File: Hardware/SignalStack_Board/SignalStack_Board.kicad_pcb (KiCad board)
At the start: 2 copper layers, 92.6 x 80.4 mm, 76 parts, among them J2 RJ45_LED_Shielded, J3 Molex_uF_SV_06, Q1 SI4156DY, Q2 SI4156DY, Q3 SI4156DY, Q4 SI4156DY, Q5 SI4156DY, Q6 SI4156DY, Q7 SI4156DY, Q8 SI4156DY, Q9 Q_PMOS_DGS, SW1 SW_Push, SW2 SW_Push, U1 OKI, U10 74LVC2G04, U2 SMAJ12CA, U3 Teensy4.1_DEV-16771, U4 TSR_1-2450, U5 IRS2005S, U6 IRS2005S, U7 74LVC2G04, U8 IRS2005S, U9 IRS2005S

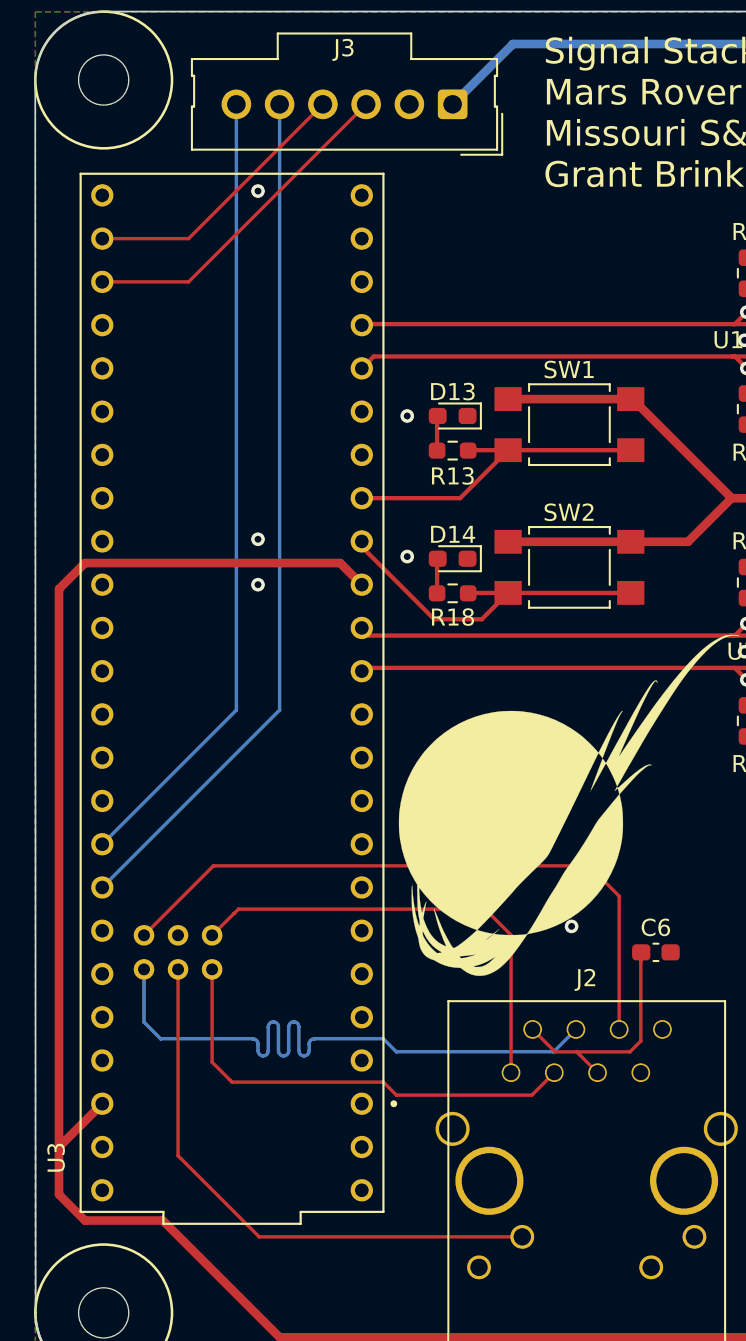
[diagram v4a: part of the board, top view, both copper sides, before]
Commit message: Added pull up resistors
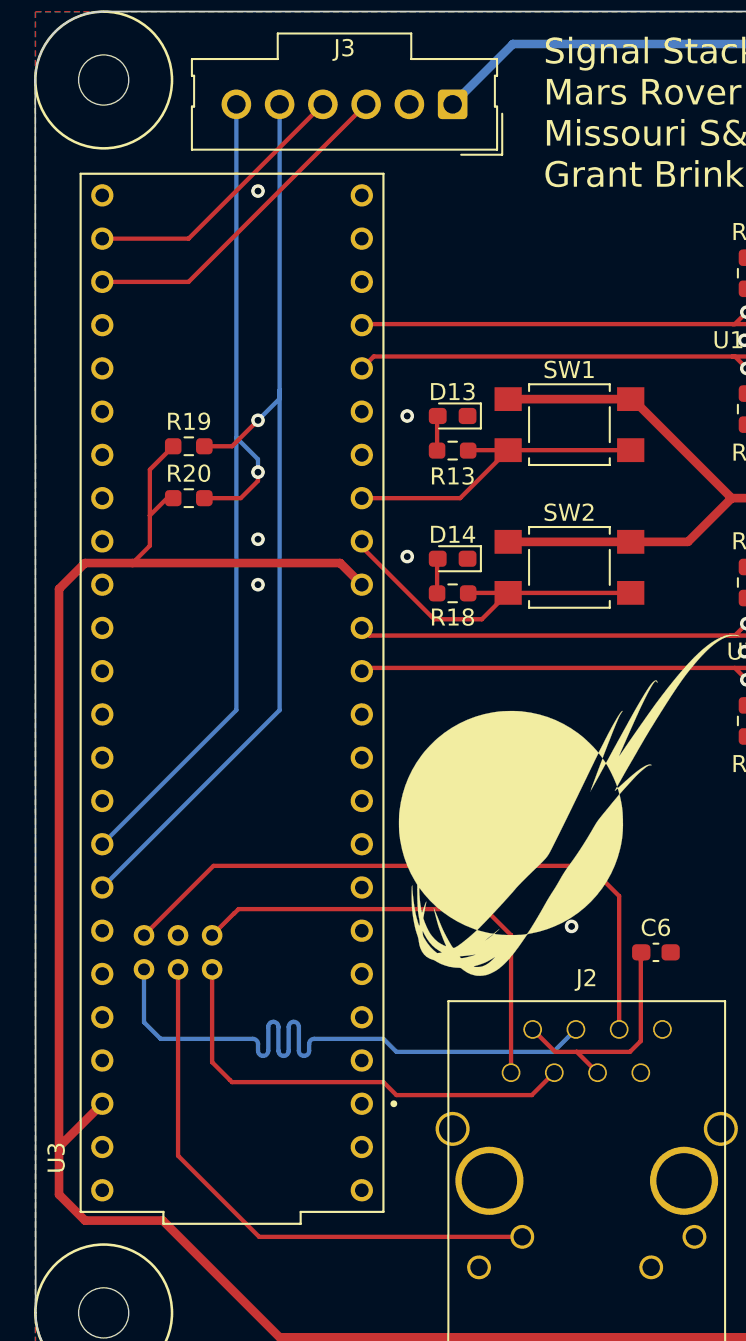
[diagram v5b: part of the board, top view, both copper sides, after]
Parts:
- added R19: 4.7k, Resistor_SMD:R_0603_1608Metric_Pad0.98x0.95mm_HandSolder, F.Cu at (121.4, 83.6)
- added R20: 4.7k, Resistor_SMD:R_0603_1608Metric_Pad0.98x0.95mm_HandSolder, F.Cu at (121.4, 86.6)
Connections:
- U3 pad R-: /RX- -> (no net)
- U3 pad T-: /TX- -> (no net)
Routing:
- net +3V3: track 261.2 -> 270.9 mm
- net I2C SDA: track 46.7 -> 53.3 mm, vias 0 -> 1
- net I2C SCL: track 50.3 -> 56.4 mm, vias 0 -> 1

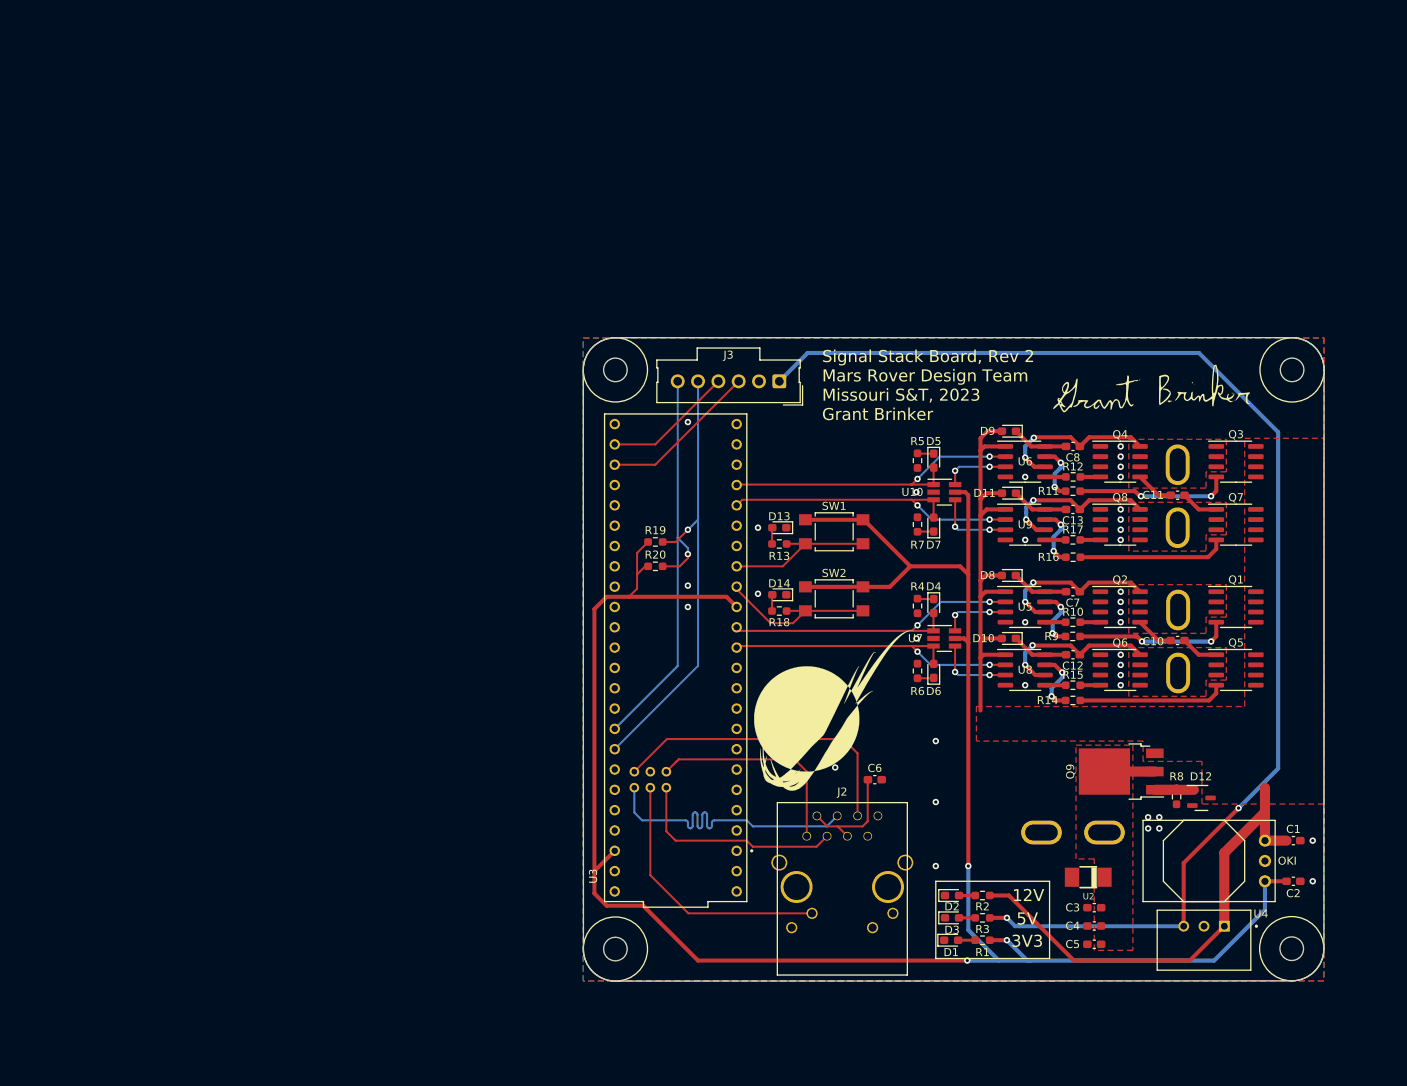
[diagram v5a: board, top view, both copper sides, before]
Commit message: Edited Signal Stack Board to be smaller
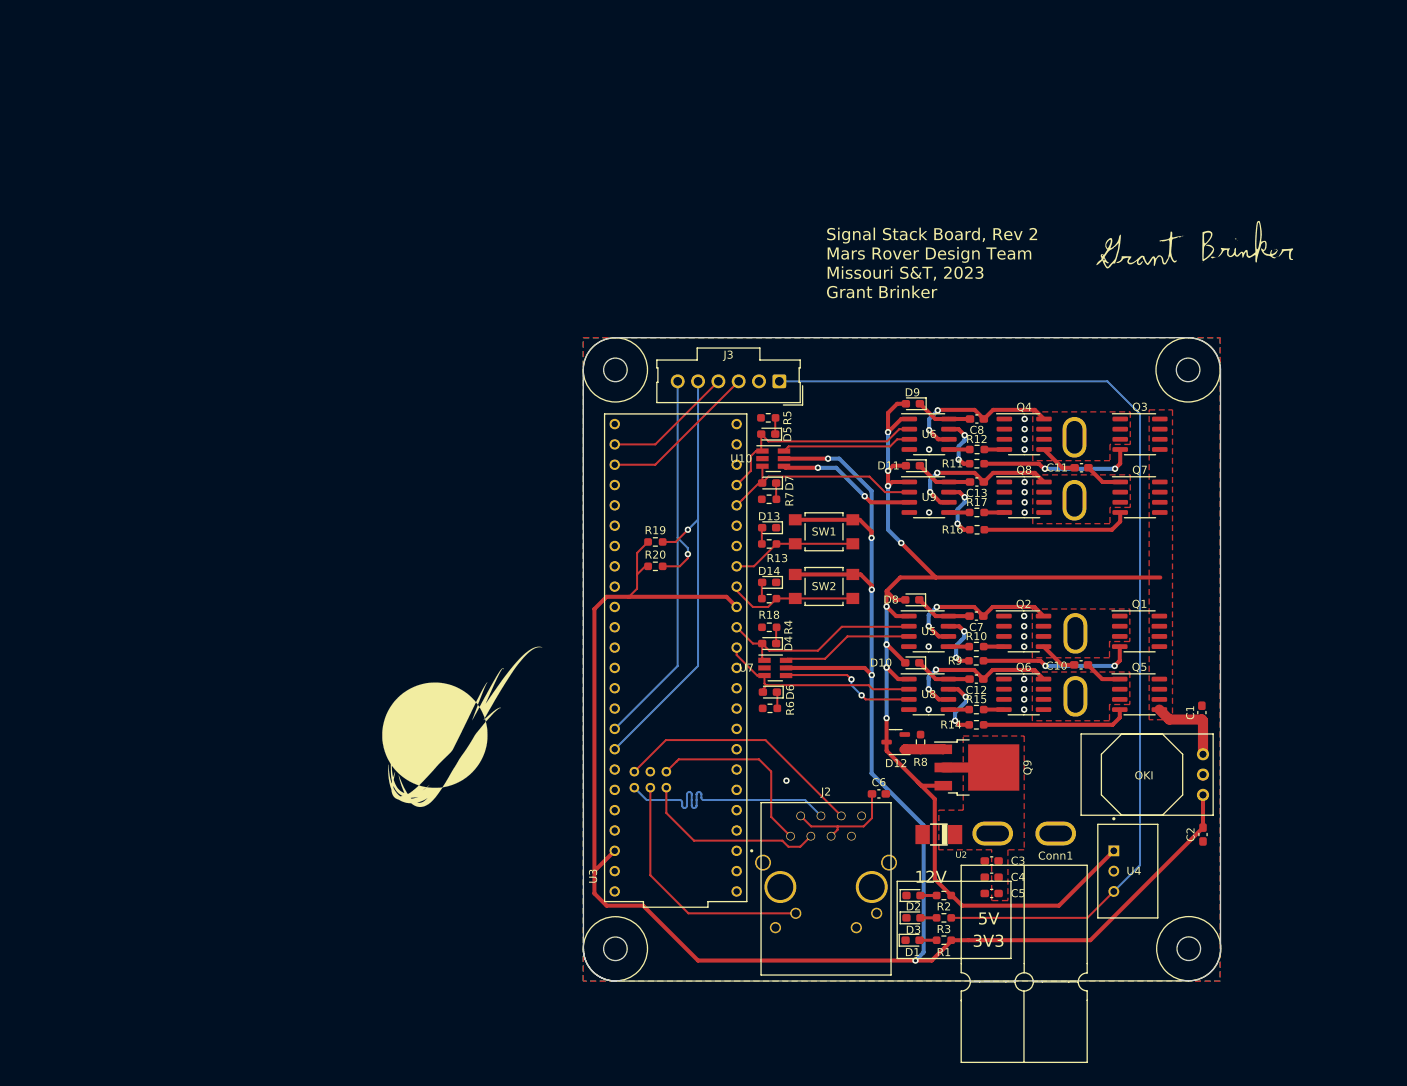
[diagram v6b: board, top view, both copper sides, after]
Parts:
- Conn1: moved to B.Cu
- moved G*** 46.5 mm to (97.3, 106.7)
- moved D12 38.9 mm to (151.4, 108.6), turned to 180 degrees
- moved R8 32.7 mm to (154.6, 108.6), turned to -90 degrees
- moved U10 21.8 mm to (136.1, 73.2)
- moved U7 21.4 mm to (136.4, 99.3)
- moved D7 21.2 mm to (135.6, 76.2), turned to 180 degrees
- moved D4 21.1 mm to (135.6, 96.3), turned to 180 degrees
- moved D5 21.0 mm to (135.5, 70.1), turned to 180 degrees
- moved D6 20.7 mm to (135.7, 102.3), turned to 180 degrees
- moved C1 19.7 mm to (189.7, 104.9), turned to 90 degrees
- moved U2 19.4 mm to (156.8, 120.1)
- moved R5 19.4 mm to (135.5, 68.1), turned to 0 degrees
- moved R6 19.0 mm to (135.7, 104.4), turned to 0 degrees
- moved R7 18.8 mm to (135.6, 78.2), turned to 0 degrees
- moved G*** 18.8 mm to (189.0, 46.5)
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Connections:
- U3 pad R-: (no net) -> /RX-
- U3 pad T-: (no net) -> /TX-
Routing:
- net +12V: track 119.3 -> 160.8 mm, vias 0 -> 8
- net +5V: track 159.2 -> 129.5 mm, vias 2 -> 0
- net Coil2_RVS: track 40.0 -> 25.8 mm, vias 2 -> 0
- net Coil1_FWD: track 40.5 -> 26.3 mm, vias 2 -> 0
- net Coil1_RVS: track 39.6 -> 26.5 mm, vias 2 -> 0
- net Coil2_FWD: track 40.0 -> 27.9 mm, vias 2 -> 0
- net Net-(U5-Pad3): track 8.42 -> 16.6 mm, vias 2 -> 0
- net Net-(U10-Pad6): track 8.22 -> 16.3 mm, vias 2 -> 0
- net Net-(U10-Pad4): track 9.82 -> 17.5 mm
- net Net-(U7-Pad4): track 9.69 -> 17.1 mm
- net /RX-: track 38.2 -> 31.4 mm
- net /RX+: track 38.0 -> 31.4 mm
- net +3V3: track 270.9 -> 265.7 mm, vias 3 -> 5
- net Motor 1: track 20.9 -> 16.6 mm
- net Motor 2: track 19.3 -> 15.7 mm
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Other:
- board size 92.6 x 80.4 mm -> 79.7 x 80.4 mm

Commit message: reduced the size of the board and fixed edgecut outlines
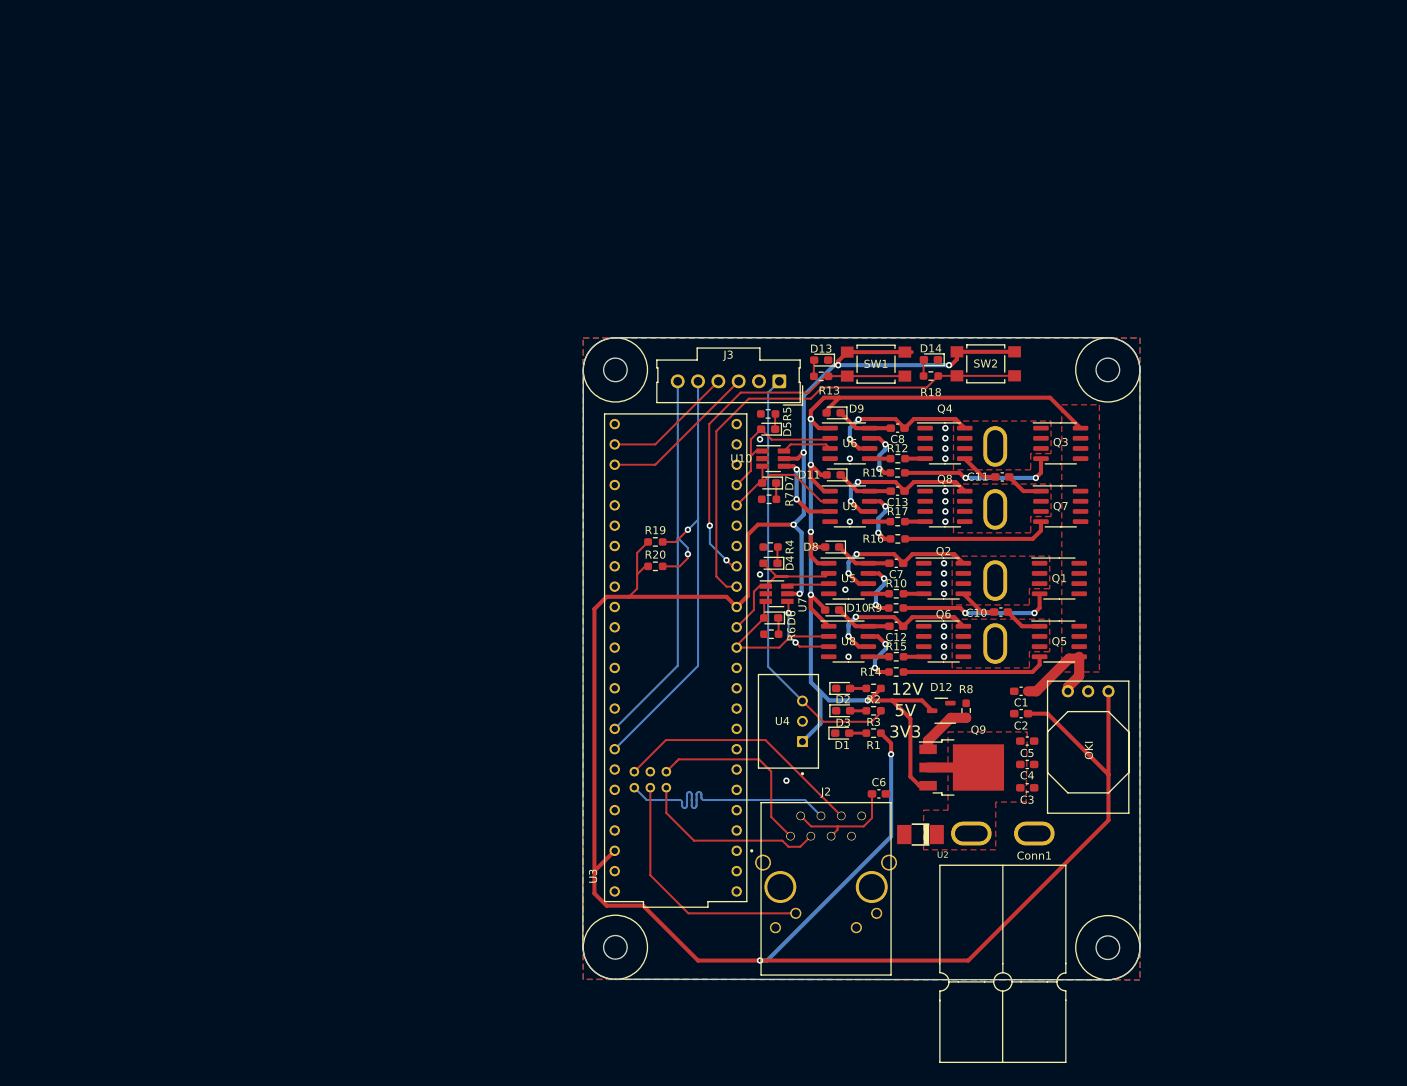
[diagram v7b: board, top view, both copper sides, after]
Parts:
- G*** (x2): moved to B.Cu
- moved G*** 65.9 mm to (159.8, 127.8), turned to 180 degrees
- moved G*** 63.0 mm to (165.4, 104.9), turned to 180 degrees
- moved U4 46.4 mm to (138.0, 106.0), turned to 90 degrees
- moved D14 34.4 mm to (155.9, 60.8)
- moved R18 34.4 mm to (155.9, 62.8)
- moved SW2 34.4 mm to (162.7, 61.3)
- moved D3 27.3 mm to (144.9, 104.7)
- moved R3 27.3 mm to (148.7, 104.7)
- moved D2 27.3 mm to (144.9, 101.9)
- moved R2 27.3 mm to (148.7, 101.9)
- moved D1 27.3 mm to (144.8, 107.5)
- moved R1 27.3 mm to (148.7, 107.5)
- moved C2 27.3 mm to (167.1, 105.0), turned to 180 degrees
- moved C1 22.7 mm to (167.1, 102.2), turned to 180 degrees
- moved D13 21.9 mm to (142.1, 60.8)
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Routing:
- net +5V: track 129.5 -> 53.9 mm
- net Motor 1: track 16.6 -> 62.0 mm
- net Motor 2: track 15.7 -> 46.5 mm, vias 0 -> 2
- net +3V3: track 265.7 -> 293.9 mm, vias 5 -> 7
- net Net-(U5-Pad3): track 16.6 -> 5.30 mm
- net Net-(U10-Pad6): track 16.3 -> 6.31 mm
- net Coil2_RVS: track 25.8 -> 16.5 mm
- net +12V: track 160.8 -> 151.8 mm, vias 8 -> 5
- net Coil2_FWD: track 27.9 -> 19.3 mm
- net Net-(U10-Pad4): track 17.5 -> 10.3 mm
- net Net-(U7-Pad4): track 17.1 -> 9.93 mm
- net Coil1_RVS: track 26.5 -> 19.4 mm
- net Coil1_FWD: track 26.3 -> 19.6 mm
- net Net-(D12-Pad2): track 4.87 -> 7.04 mm
- net GND: vias 21 -> 23
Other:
- board size 79.7 x 80.4 mm -> 69.6 x 80.3 mm

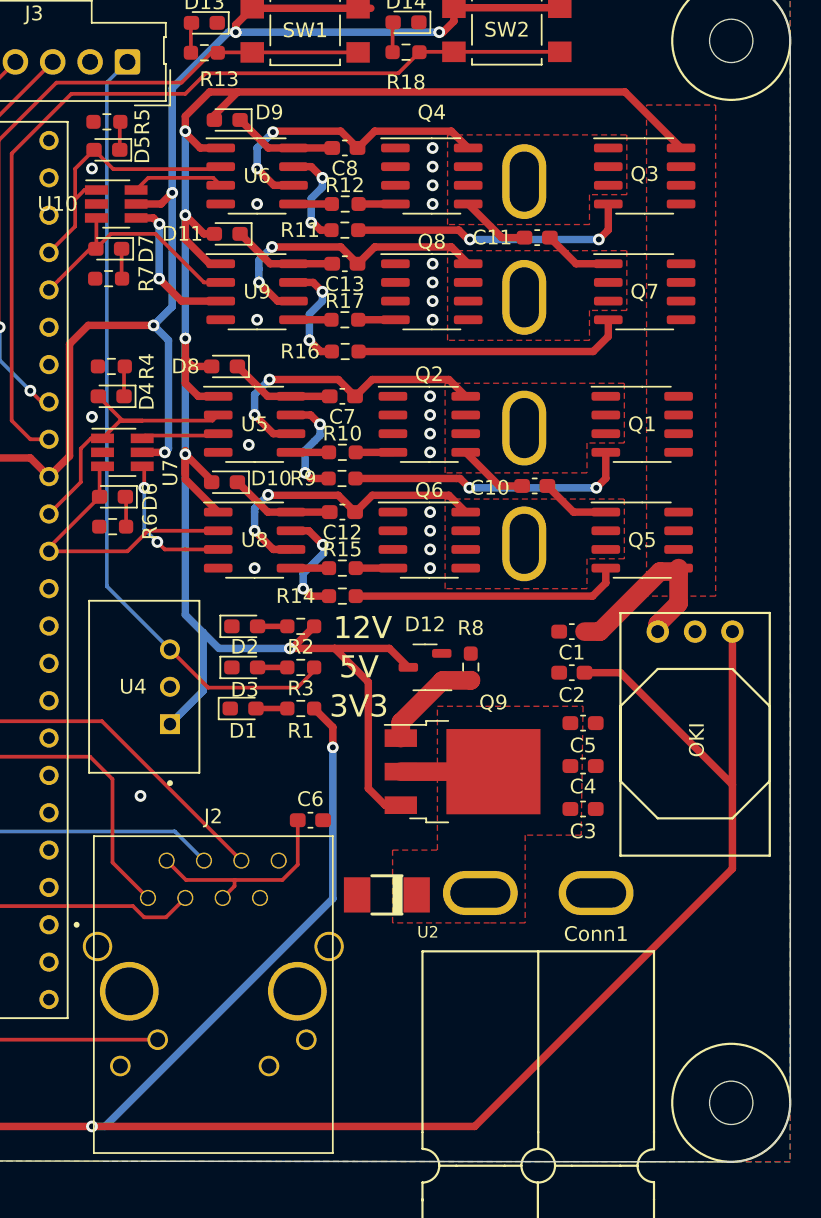
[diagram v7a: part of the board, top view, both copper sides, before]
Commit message: rotated qmos and removed a back 12 v plane
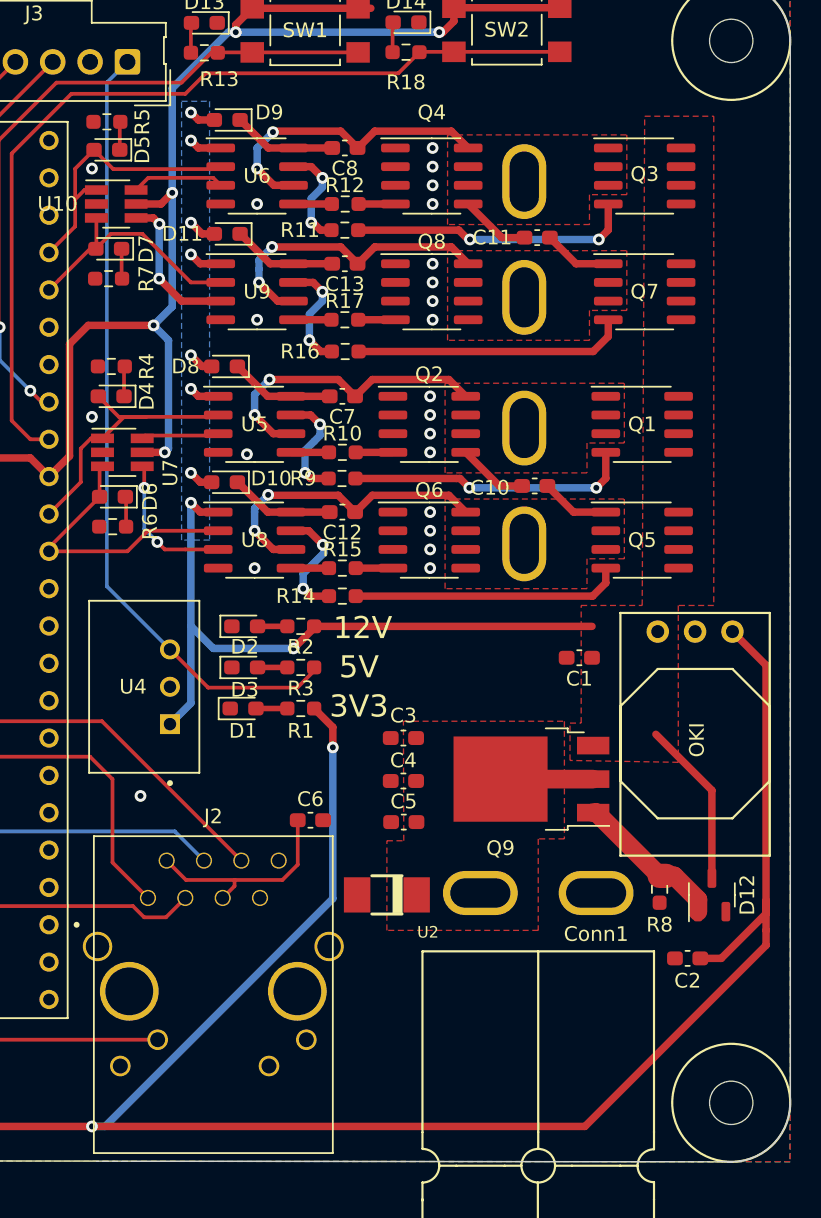
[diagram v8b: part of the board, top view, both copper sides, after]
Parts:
- moved D12 24.9 mm to (176.7, 120.1), turned to 90 degrees
- moved C2 21.0 mm to (175.0, 124.5)
- moved R8 19.8 mm to (173.1, 119.8), turned to 90 degrees
- moved C5 13.9 mm to (155.7, 115.2), turned to 180 degrees
- moved C3 13.1 mm to (155.7, 109.5), turned to 180 degrees
- moved C4 12.3 mm to (155.7, 112.4), turned to 180 degrees
- moved Q9 4.71 mm to (164.4, 112.3), turned to 180 degrees
- moved C1 1.85 mm to (167.6, 104.0)
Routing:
- net +12V: track 151.8 -> 72.0 mm, vias 5 -> 9
- net Net-(D12-Pad2): track 7.04 -> 10.4 mm
- added copper zone on B.Cu, net +12V
